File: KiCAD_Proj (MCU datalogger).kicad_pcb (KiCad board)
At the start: 2 copper layers, 52.3 x 34.7 mm, 31 parts, among them J1 Conn_01x04_Pin, J2 Conn_01x09_Pin, J3 Conn_01x04_Pin, J4 Conn_02x03_Counter_Clockwise, U1 24LC1025-I_SM, U2 DS1337S_, U3 24LC1025-I_SM, U4 ATMEGA328P-AU, Y1 32.768 KHz, Y2 16MHz

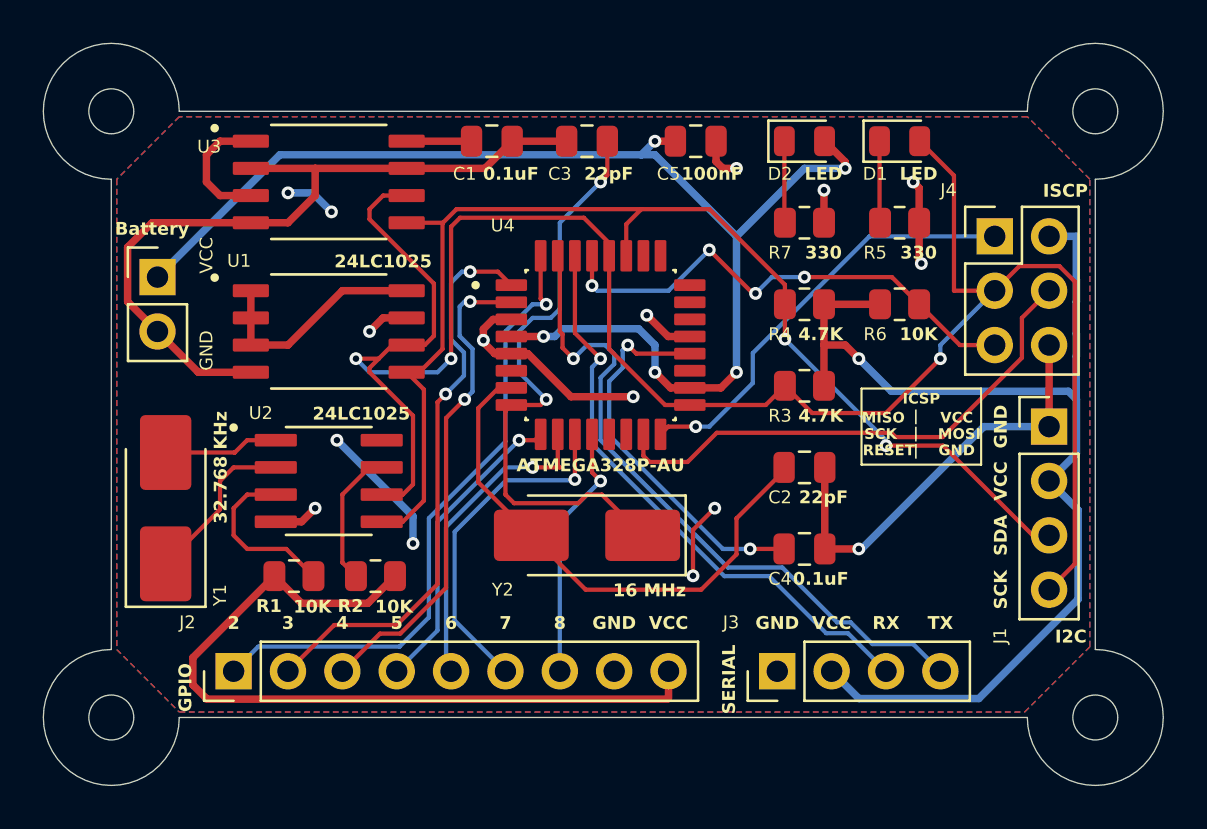
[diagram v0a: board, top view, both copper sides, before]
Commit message: Fixing the bug on PCB.
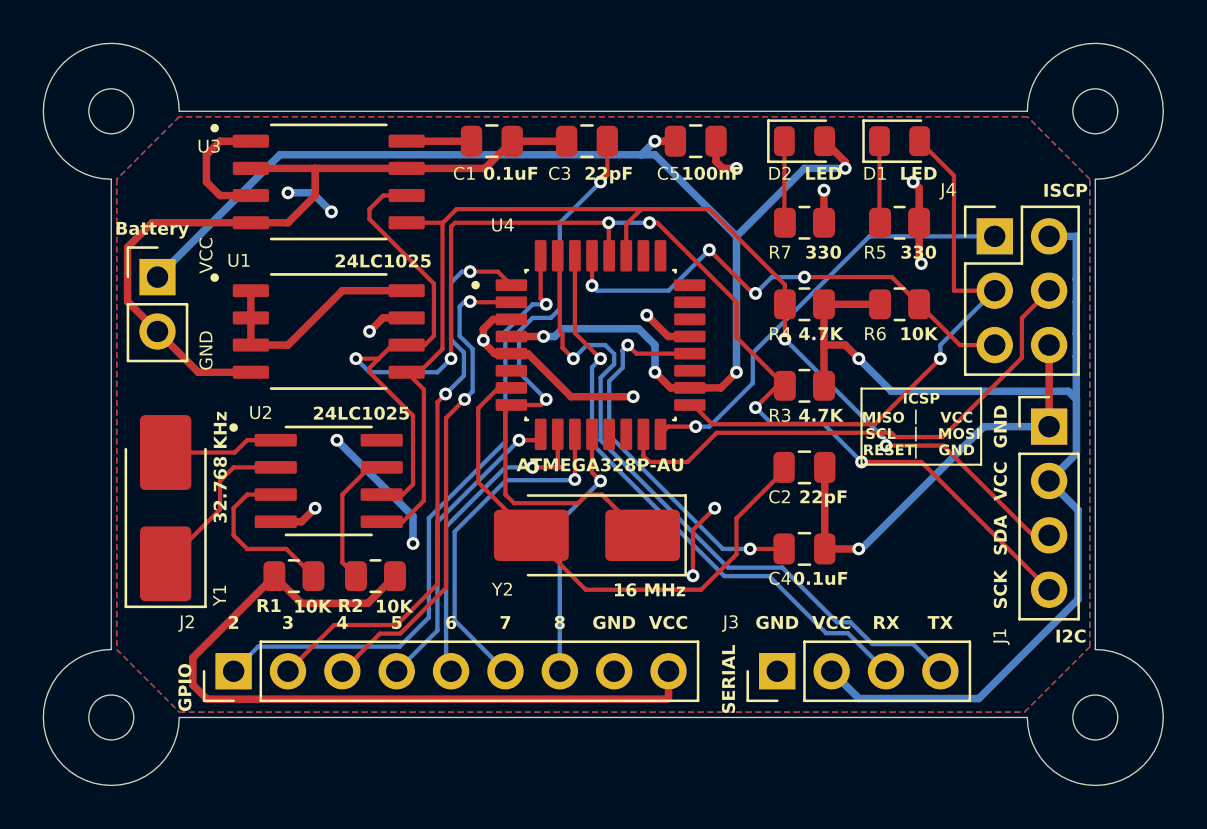
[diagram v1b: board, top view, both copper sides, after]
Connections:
- J1 pad 4: /SCK -> /SCL
- R3 pad 2: /SCK -> /SCL
- U1 pad 6: /SCK -> /SCL
- U2 pad 6: /SCK -> /SCL
- U3 pad 6: /SCK -> /SCL
- U4 pad 28: /SCK -> /SCL
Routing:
- net /SCL: track 0.00 -> 73.9 mm, vias 0 -> 6
- net /SCK: track 97.6 -> 27.1 mm, vias 3 -> 1
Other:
- board text added: "SCL"
